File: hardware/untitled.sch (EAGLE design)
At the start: 44 parts, among them IC2 LM1117IMPX-3.3, U4 microSD, Y1 CRYSTAL-GROUNDEDSMD-5X3.2

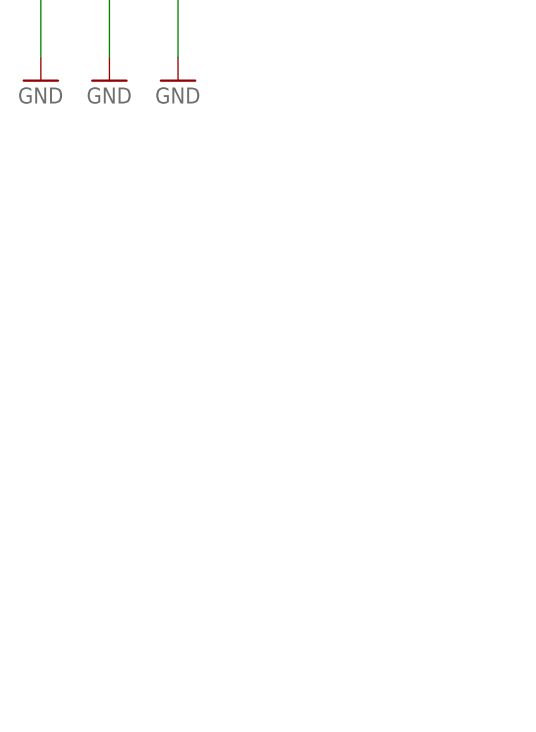
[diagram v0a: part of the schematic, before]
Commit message: Reset fix
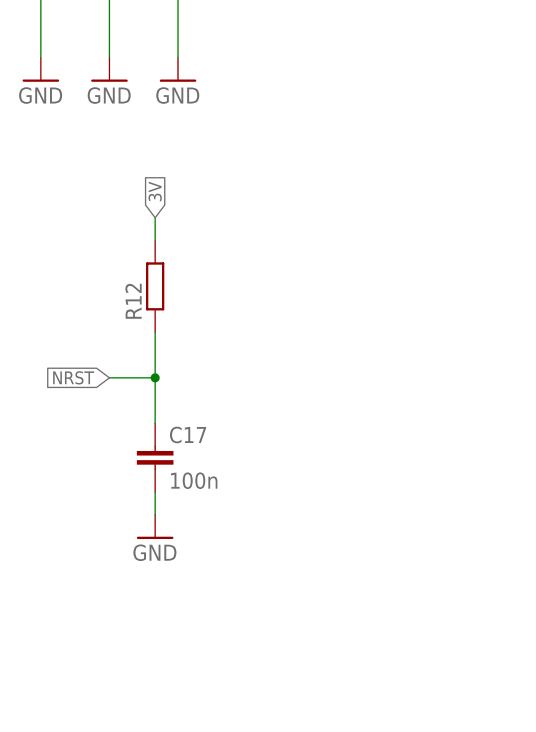
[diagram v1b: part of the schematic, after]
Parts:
- added C17: 100n, rcl:C-EUC0603
- added R12: (no value), rcl:R-EU_R0603
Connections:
- net 3V: now also R12.2
- net GND: now also C17.2
- net NRST: now also C17.1, R12.1
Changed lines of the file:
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@@
 <part name="C16" library="rcl" deviceset="CPOL-EU" device="SMCB"/>
 <part name="GND21" library="supply1" deviceset="GND" device=""/>
+<part name="R12" library="rcl" deviceset="R-EU_" device="R0603"/>
+<part name="C17" library="rcl" deviceset="C-EU" device="C0603" value="100n"/>
+<part name="GND24" library="supply1" deviceset="GND" device=""/>
 </parts>
 <sheets>
@@
 <instance part="C16" gate="G$1" x="157.48" y="139.7"/>
 <instance part="GND21" gate="1" x="157.48" y="129.54"/>
+<instance part="R12" gate="G$1" x="-66.04" y="22.86" rot="R90"/>
+<instance part="C17" gate="G$1" x="-66.04" y="5.08"/>
+<instance part="GND24" gate="1" x="-66.04" y="-5.08"/>
 </instances>
 <busses>
@@
 <pinref part="GND21" gate="1" pin="GND"/>
 <wire x1="157.48" y1="132.08" x2="157.48" y2="134.62" width="0.1524" layer="91"/>
+</segment>
+<segment>
+<pinref part="C17" gate="G$1" pin="2"/>
+<pinref part="GND24" gate="1" pin="GND"/>
+<wire x1="-66.04" y1="-2.54" x2="-66.04" y2="0" width="0.1524" layer="91"/>
 </segment>
 </net>
@@
 <junction x="345.44" y="104.14"/>
 </segment>
+<segment>
+<pinref part="R12" gate="G$1" pin="2"/>
+<wire x1="-66.04" y1="27.94" x2="-66.04" y2="30.48" width="0.1524" layer="91"/>
+<label x="-66.04" y="30.48" size="1.4224" layer="95" rot="R90" xref="yes"/>
+</segment>
 </net>
 <net name="5V" class="0">
@@
 <label x="20.32" y="99.06" size="1.4224" layer="95" rot="R90" xref="yes"/>
 </segment>
-</net>
+<segment>
+<pinref part="R12" gate="G$1" pin="1"/>
+<wire x1="-66.04" y1="12.7" x2="-71.12" y2="12.7" width="0.1524" layer="91"/>
+<wire x1="-66.04" y1="17.78" x2="-66.04" y2="12.7" width="0.1524" layer="91"/>
+<junction x="-66.04" y="12.7"/>
+<pinref part="C17" gate="G$1" pin="1"/>
+<wire x1="-66.04" y1="12.7" x2="-66.04" y2="7.62" width="0.1524" layer="91"/>
+<label x="-71.12" y="12.7" size="1.4224" layer="95" rot="R180" xref="yes"/>
+</segment>
+</net>

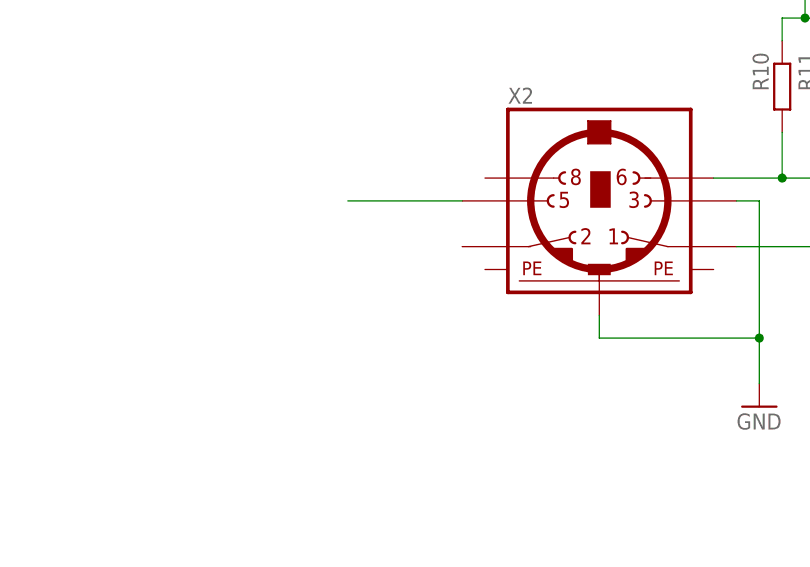
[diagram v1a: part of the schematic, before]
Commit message: Capacitor at PS/2 socket
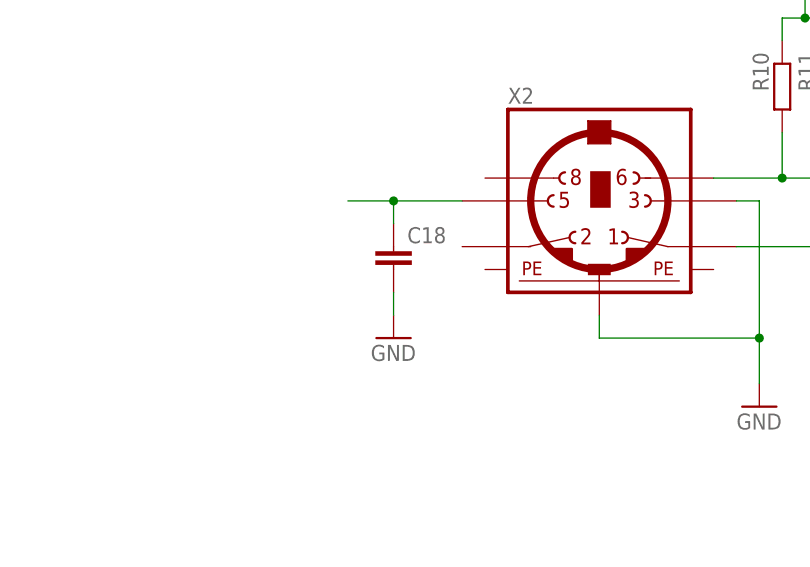
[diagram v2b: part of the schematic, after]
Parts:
- added C18: (no value), rcl:C-EUC0603
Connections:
- net 5V: now also C18.1
- net GND: now also C18.2
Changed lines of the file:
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@@
 <part name="C17" library="rcl" deviceset="C-EU" device="C0603" value="100n"/>
 <part name="GND24" library="supply1" deviceset="GND" device=""/>
+<part name="C18" library="rcl" deviceset="C-EU" device="C0603"/>
+<part name="GND22" library="supply1" deviceset="GND" device=""/>
 </parts>
 <sheets>
@@
 <instance part="C17" gate="G$1" x="-66.04" y="5.08"/>
 <instance part="GND24" gate="1" x="-66.04" y="-5.08"/>
+<instance part="C18" gate="G$1" x="299.72" y="78.74"/>
+<instance part="GND22" gate="1" x="299.72" y="68.58"/>
 </instances>
 <busses>
@@
 <pinref part="GND24" gate="1" pin="GND"/>
 <wire x1="-66.04" y1="-2.54" x2="-66.04" y2="0" width="0.1524" layer="91"/>
+</segment>
+<segment>
+<pinref part="C18" gate="G$1" pin="2"/>
+<pinref part="GND22" gate="1" pin="GND"/>
+<wire x1="299.72" y1="71.12" x2="299.72" y2="73.66" width="0.1524" layer="91"/>
 </segment>
 </net>
@@
 <segment>
 <pinref part="X2" gate="G$1" pin="5"/>
-<wire x1="307.34" y1="83.82" x2="294.64" y2="83.82" width="0.1524" layer="91"/>
-</segment>
-</net>
+<wire x1="307.34" y1="83.82" x2="299.72" y2="83.82" width="0.1524" layer="91"/>
+<pinref part="C18" gate="G$1" pin="1"/>
+<wire x1="299.72" y1="83.82" x2="294.64" y2="83.82" width="0.1524" layer="91"/>
+<wire x1="299.72" y1="81.28" x2="299.72" y2="83.82" width="0.1524" layer="91"/>
+<junction x="299.72" y="83.82"/>
+</segment>
+</net>

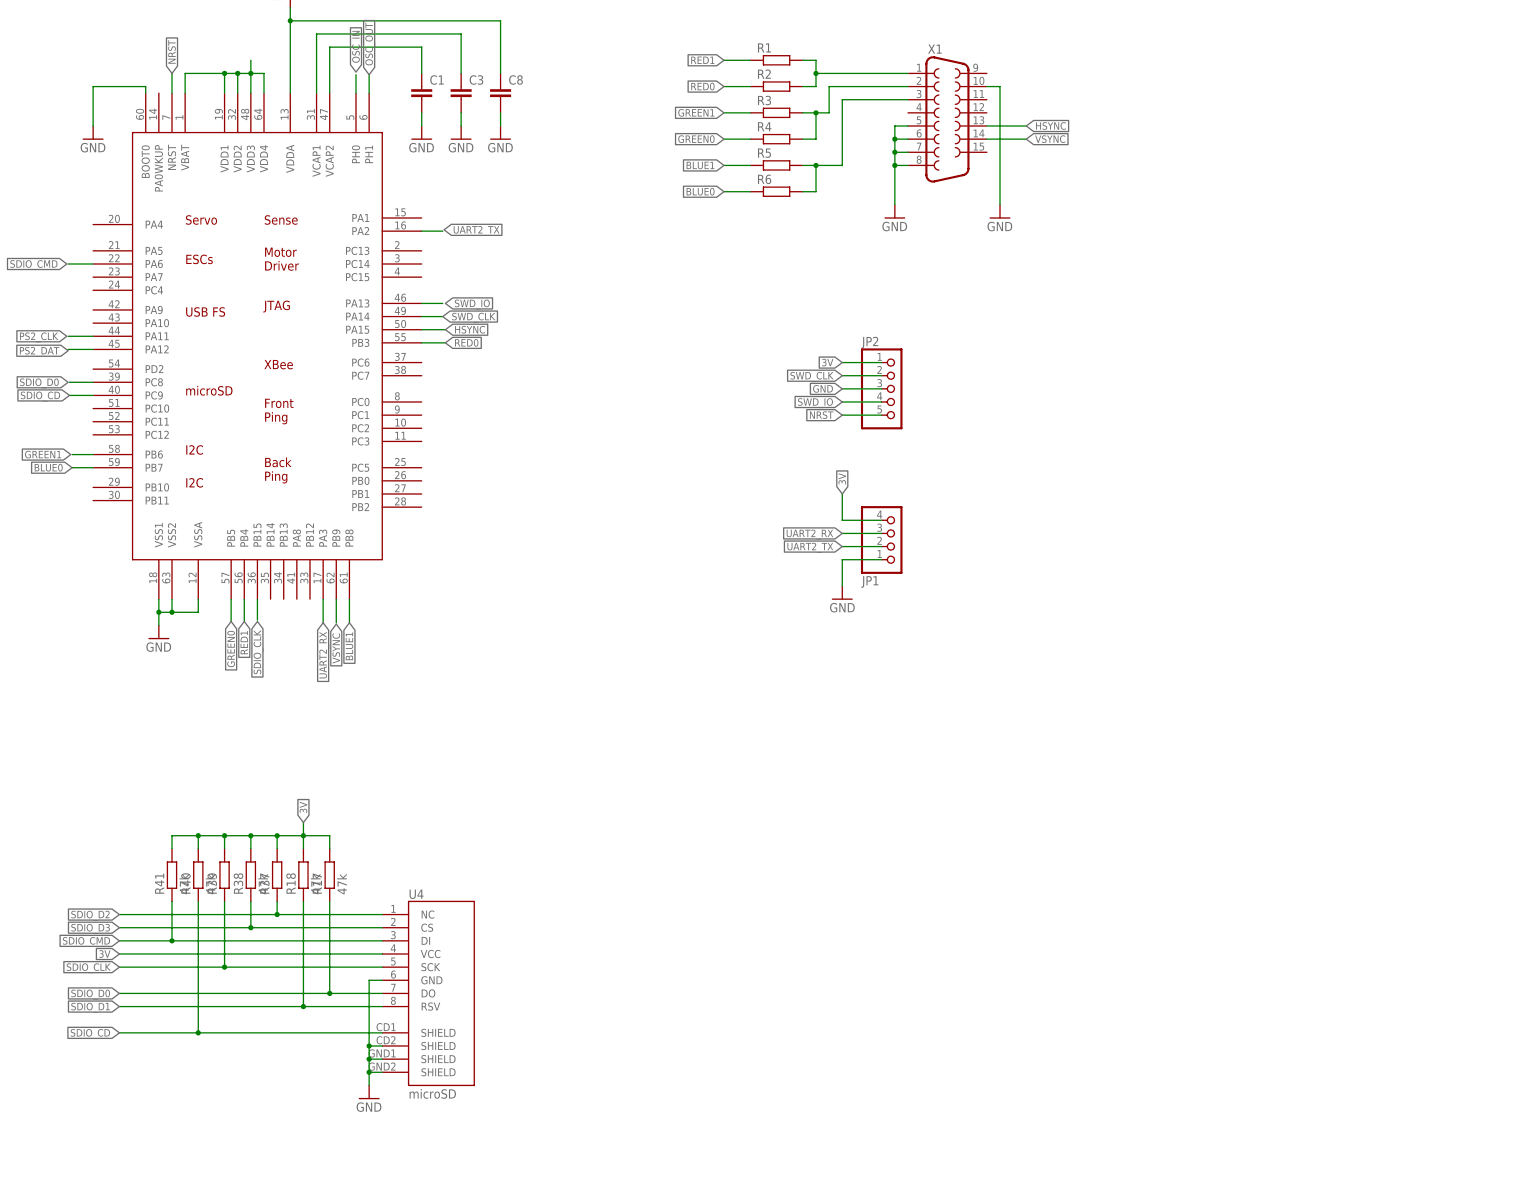
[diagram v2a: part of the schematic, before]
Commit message: Proper MCU footprint used
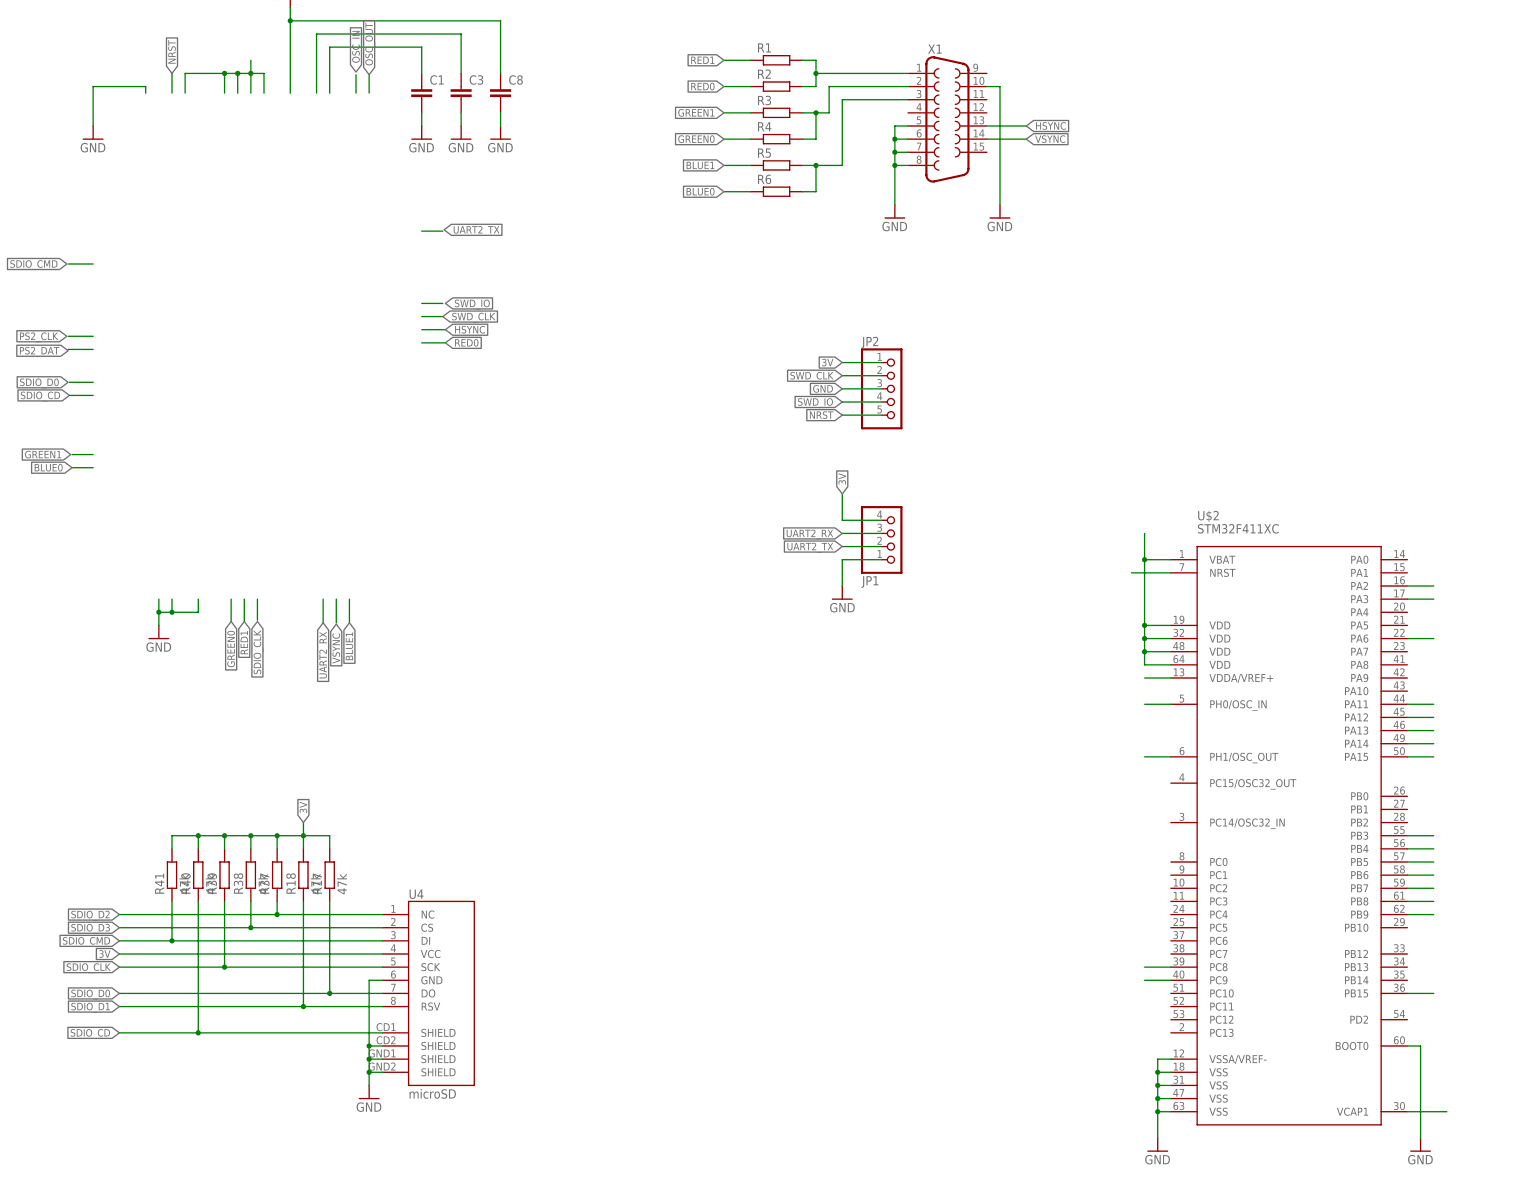
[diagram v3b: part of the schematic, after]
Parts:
- removed U$1: STM32F4R_64PIN_FOXCAR, stm32f4:STM32F4R_64PIN_FOXCAR
- added U$2: STM32F411XC, stm32f411:STM32F411XC
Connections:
- net 3V: now also U$2.VBAT, U$2.VDD@1, U$2.VDD@2, U$2.VDD@3, U$2.VDD@4; no longer U$1.VBAT, U$1.VDD1, U$1.VDD2, U$1.VDD3, U$1.VDD4
- net BLUE0: now also U$2.PB7; no longer U$1.PB7
- net BLUE1: now also U$2.PB8; no longer U$1.PB8
- net GND: now also U$2.BOOT0, U$2.VSS@1, U$2.VSS@2, U$2.VSS@3, U$2.VSS@4, U$2.VSSA/VREF-; no longer U$1.BOOT0, U$1.VSS1, U$1.VSS2, U$1.VSSA
- net GREEN0: now also U$2.PB5; no longer U$1.PB5
- net GREEN1: now also U$2.PB6; no longer U$1.PB6
- net HSYNC: now also U$2.PA15; no longer U$1.PA15
- net N$6: now also U$2.VDDA/VREF+; no longer U$1.VDDA
- net N$7: no longer U$1.VCAP2
- net N$8: now also U$2.VCAP1; no longer U$1.VCAP1
- net NRST: now also U$2.NRST; no longer U$1.NRST
- net OSC_IN: now also U$2.PH0/OSC_IN; no longer U$1.PH0
- net OSC_OUT: now also U$2.PH1/OSC_OUT; no longer U$1.PH1
- net PS2_CLK: now also U$2.PA11; no longer U$1.PA11
- net PS2_DAT: now also U$2.PA12; no longer U$1.PA12
- net RED0: now also U$2.PB3; no longer U$1.PB3
- net RED1: now also U$2.PB4; no longer U$1.PB4
- net SDIO_CD: now also U$2.PC9; no longer U$1.PC9
- net SDIO_CLK: now also U$2.PB15; no longer U$1.PB15
- net SDIO_CMD: now also U$2.PA6; no longer U$1.PA6
- net SDIO_D0: now also U$2.PC8; no longer U$1.PC8
- net SWD_CLK: now also U$2.PA14; no longer U$1.PA14
- net SWD_IO: now also U$2.PA13; no longer U$1.PA13
- net UART2_RX: now also U$2.PA3; no longer U$1.PA3
- net UART2_TX: now also U$2.PA2; no longer U$1.PA2
- net VSYNC: now also U$2.PB9; no longer U$1.PB9

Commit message: Minor adjustment
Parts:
- removed C1: (no value), rcl:C-EUC0603
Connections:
- removed net N$7: C1.1
- net GND: no longer C1.2
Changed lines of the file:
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@@
 <part name="GND4" library="supply1" deviceset="GND" device=""/>
 <part name="GND5" library="supply1" deviceset="GND" device=""/>
-<part name="C1" library="rcl" deviceset="C-EU" device="C0603"/>
 <part name="C3" library="rcl" deviceset="C-EU" device="C0603"/>
-<part name="GND6" library="supply1" deviceset="GND" device=""/>
 <part name="GND7" library="supply1" deviceset="GND" device=""/>
 <part name="U4" library="SparkFun-Connectors" deviceset="USD-SOCKET" device="USD" value="microSD"/>
@@
 <instance part="GND4" gate="1" x="17.78" y="-10.16"/>
 <instance part="GND5" gate="1" x="5.08" y="86.36"/>
-<instance part="C1" gate="G$1" x="68.58" y="96.52"/>
 <instance part="C3" gate="G$1" x="76.2" y="96.52"/>
-<instance part="GND6" gate="1" x="68.58" y="86.36"/>
 <instance part="GND7" gate="1" x="76.2" y="86.36"/>
 <instance part="U4" gate="G$1" x="68.58" y="-76.2"/>
@@
 </segment>
 <segment>
-<pinref part="C1" gate="G$1" pin="2"/>
-<pinref part="GND6" gate="1" pin="GND"/>
-<wire x1="68.58" y1="88.9" x2="68.58" y2="91.44" width="0.1524" layer="91"/>
-</segment>
-<segment>
 <pinref part="C3" gate="G$1" pin="2"/>
 <pinref part="GND7" gate="1" pin="GND"/>
@@
 </segment>
 </net>
-<net name="N$7" class="0">
-<segment>
-<wire x1="50.8" y1="95.25" x2="50.8" y2="104.14" width="0.1524" layer="91"/>
-<pinref part="C1" gate="G$1" pin="1"/>
-<wire x1="50.8" y1="104.14" x2="68.58" y2="104.14" width="0.1524" layer="91"/>
-<wire x1="68.58" y1="104.14" x2="68.58" y2="99.06" width="0.1524" layer="91"/>
-</segment>
-</net>
